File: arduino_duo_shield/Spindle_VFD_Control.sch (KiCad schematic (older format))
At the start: 25 parts, among them K2 JQC-3F, K3 JQC-3F, Q3 2N7000, Q4 BS250, Q5 2N7000, Q6 2N7000, U7 PC817, U8 PC817, U9 PC817

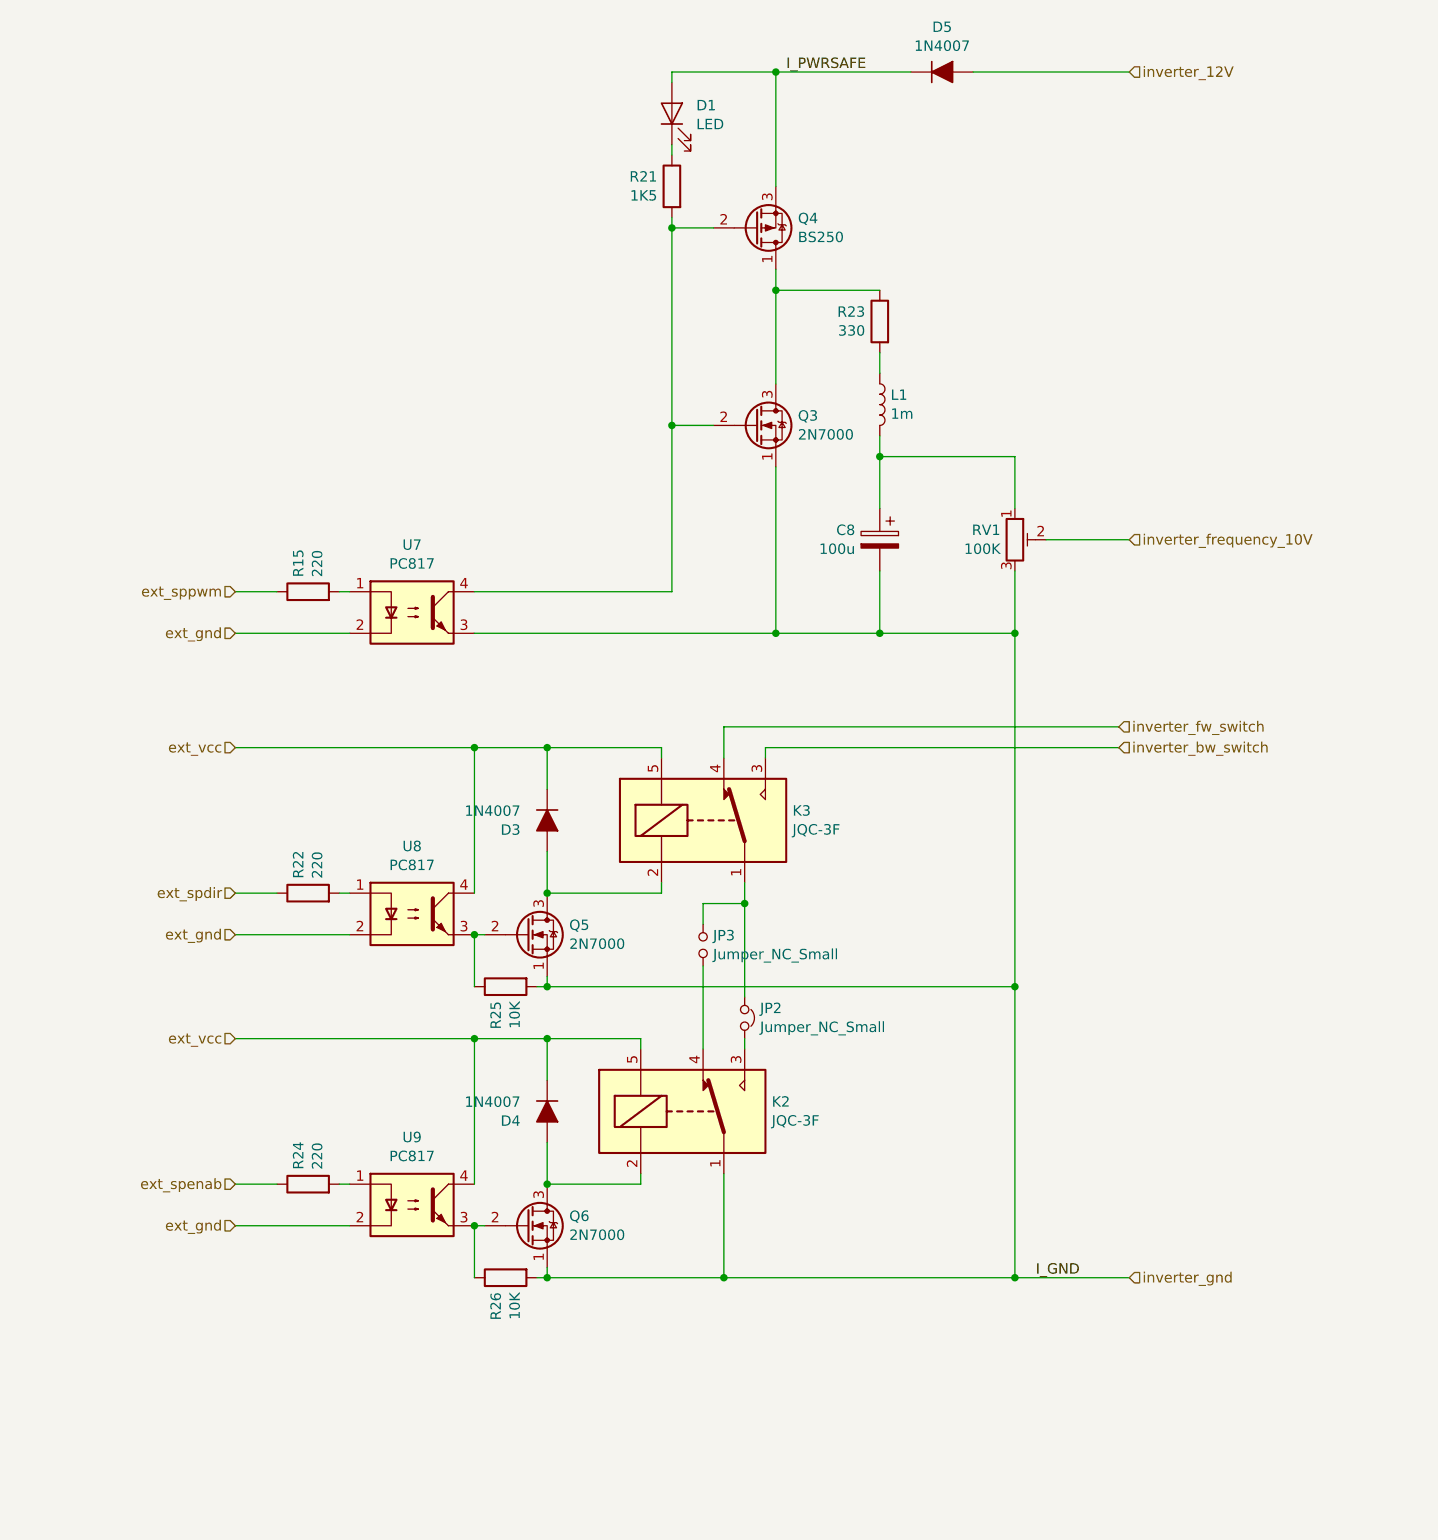
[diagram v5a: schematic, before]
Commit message: Add voltage follower as end stage of spindle control
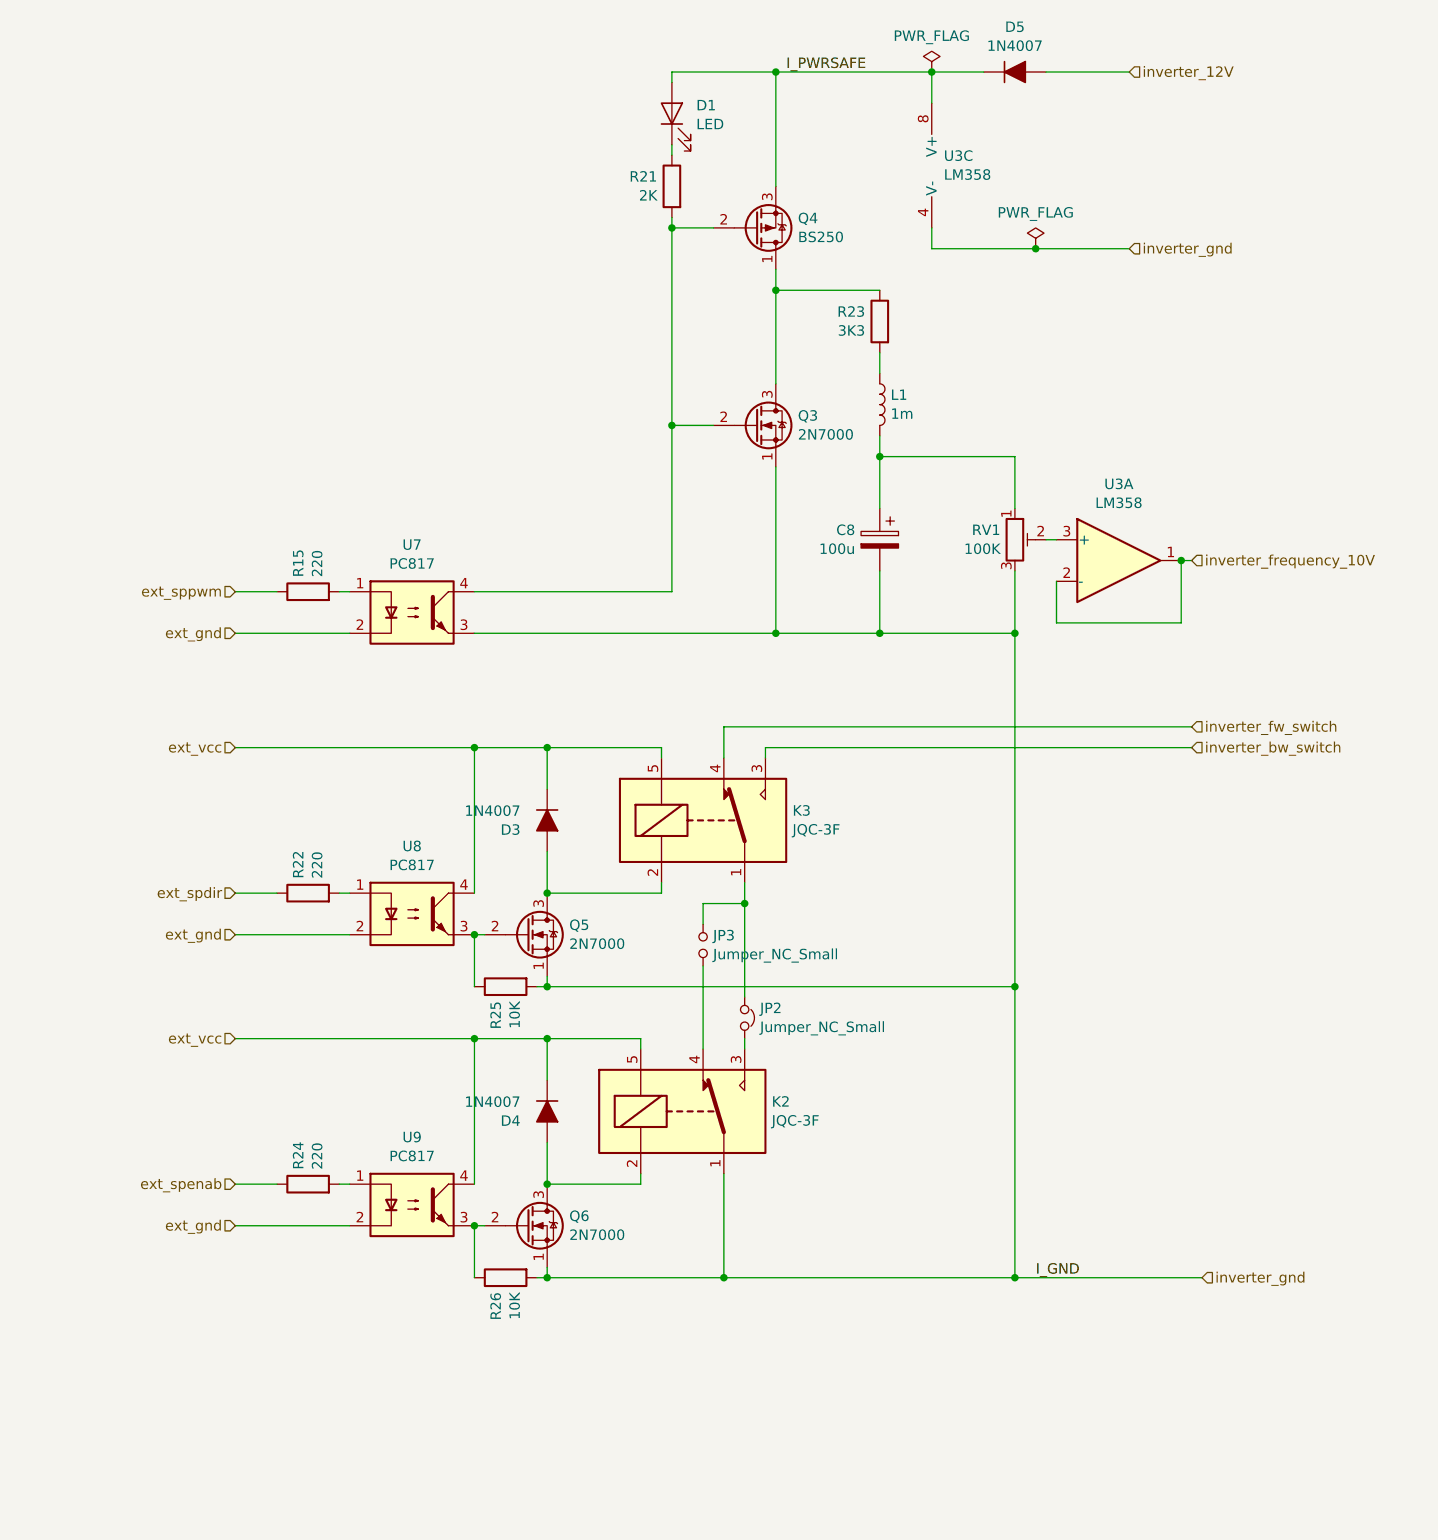
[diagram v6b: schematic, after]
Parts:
- added U3: LM358, Package_DIP:DIP-8_W7.62mm_Socket, symbol Amplifier_Operational:LM358
- R21: value 1K5 -> 2K
- R23: value 330 -> 3K3
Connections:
- net I_PWRSAFE: now also U3.8 (V+)
- net inverter_frequency_10V: now also U3.1, U3.2 (-); no longer RV1.2
- net inverter_gnd: now also U3.4 (V-)
- new net: RV1.2, U3.3 (+)
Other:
- moved on the sheet: D5
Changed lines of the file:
@@
 AR Path="/5DD17641/5DD6EE33" Ref="R23"  Part="1"
 F 0 "R23" H 5120 2046 50  0000 L CNN
-F 1 "330" H 5120 1955 50  0000 L CNN
+F 1 "3K3" H 5120 1955 50  0000 L CNN
 F 2 "Resistor_THT:R_Axial_DIN0309_L9.0mm_D3.2mm_P12.70mm_Horizontal" V 4980 2000 50  0001 C CNN
 F 3 "~" H 5050 2000 50  0001 C CNN
@@
 Wire Wire Line
 	2450 3300 2500 3300
-Text HLabel 6250 3050 2    50   Input ~ 0
+Text HLabel 6550 3150 2    50   Input ~ 0
 inverter_frequency_10V
 $Comp
@@
 AR Path="/5DD17641/5DD63534" Ref="R21"  Part="1"
 F 0 "R21" H 4120 1396 50  0000 L CNN
-F 1 "1K5" H 4120 1305 50  0000 L CNN
+F 1 "2K" H 4120 1305 50  0000 L CNN
 F 2 "Resistor_THT:R_Axial_DIN0207_L6.3mm_D2.5mm_P7.62mm_Horizontal" V 3980 1350 50  0001 C CNN
 F 3 "~" H 4050 1350 50  0001 C CNN
@@
 	4250 2500 4050 2500
 Wire Wire Line
-	6250 800  5500 800
-Wire Wire Line
 	4550 1350 4550 800
 Connection ~ 4550 800
@@
 	5050 3500 5700 3500
 Connection ~ 5050 3500
-Wire Wire Line
-	5850 3050 6250 3050
 $Comp
 L Device:R_POT_TRIM RV1
@@
 L Device:D_ALT D5
 U 1 1 5DE3902E
-P 5350 800
-F 0 "D5" H 5350 1016 50  0000 C CNN
-F 1 "1N4007" H 5350 925 50  0000 C CNN
-F 2 "Diode_THT:D_A-405_P7.62mm_Horizontal" H 5350 800 50  0001 C CNN
-F 3 "~" H 5350 800 50  0001 C CNN
-	1    5350 800
-	1    0    0    -1
-$EndComp
-Wire Wire Line
-	5200 800  4550 800
+P 5700 800
+F 0 "D5" H 5700 1016 50  0000 C CNN
+F 1 "1N4007" H 5700 925 50  0000 C CNN
+F 2 "Diode_THT:D_A-405_P7.62mm_Horizontal" H 5700 800 50  0001 C CNN
+F 3 "~" H 5700 800 50  0001 C CNN
+	1    5700 800
+	1    0    0    -1
+$EndComp
 $Comp
 L Relay:G5LE-1 K?
@@
 Wire Wire Line
 	3100 5450 3450 5450
-Text HLabel 6200 3950 2    50   Input ~ 0
+Text HLabel 6550 3950 2    50   Input ~ 0
 inverter_fw_switch
-Text HLabel 6200 4050 2    50   Input ~ 0
+Text HLabel 6550 4050 2    50   Input ~ 0
 inverter_bw_switch
-Text HLabel 6250 6600 2    50   Input ~ 0
+Text HLabel 6600 6600 2    50   Input ~ 0
 inverter_gnd
 Wire Wire Line
@@
 	1950 6350 2500 6350
 Wire Wire Line
-	6200 3950 4300 3950
+	6550 3950 4300 3950
 Wire Wire Line
 	4300 3950 4300 4100
 Wire Wire Line
-	6200 4050 4500 4050
+	6550 4050 4500 4050
 Wire Wire Line
 	4500 4050 4500 4100
@@
 Connection ~ 5700 6600
 Wire Wire Line
-	5700 6600 6250 6600
+	5700 6600 6600 6600
 Wire Wire Line
 	3450 5450 3450 5650
@@
 	0    -1   -1   0
 $EndComp
+$Comp
+L Amplifier_Operational:LM358 U3
+U 1 1 5E168C58
+P 6200 3150
+F 0 "U3" H 6200 3517 50  0000 C CNN
+F 1 "LM358" H 6200 3426 50  0000 C CNN
+F 2 "Package_DIP:DIP-8_W7.62mm_Socket" H 6200 3150 50  0001 C CNN
+F 3 "http://www.ti.com/lit/ds/symlink/lm2904-n.pdf" H 6200 3150 50  0001 C CNN
+	1    6200 3150
+	1    0    0    -1
+$EndComp
+Wire Wire Line
+	6500 3150 6550 3150
+Wire Wire Line
+	5850 3050 5900 3050
+Wire Wire Line
+	6500 3150 6500 3450
+Wire Wire Line
+	6500 3450 5900 3450
+Wire Wire Line
+	5900 3450 5900 3250
+Connection ~ 6500 3150
+Connection ~ 5300 800
+Wire Wire Line
+	5300 800  4550 800
+Text HLabel 6250 1650 2    50   Input ~ 0
+inverter_gnd
+Wire Wire Line
+	5550 800  5300 800
+Wire Wire Line
+	5850 800  6250 800
+Wire Wire Line
+	5300 800  5300 950
+Wire Wire Line
+	5300 1650 5800 1650
+Wire Wire Line
+	5300 1650 5300 1550
+$Comp
+L Amplifier_Operational:LM358 U3
+U 3 1 5E193DCF
+P 5400 1250
+F 0 "U3" H 5358 1296 50  0000 L CNN
+F 1 "LM358" H 5358 1205 50  0000 L CNN
+F 2 "Package_DIP:DIP-8_W7.62mm_Socket" H 5400 1250 50  0001 C CNN
+F 3 "http://www.ti.com/lit/ds/symlink/lm2904-n.pdf" H 5400 1250 50  0001 C CNN
+	3    5400 1250
+	1    0    0    -1
+$EndComp
+$Comp
+L power:PWR_FLAG #FLG0101
+U 1 1 5E16F505
+P 5300 800
+F 0 "#FLG0101" H 5300 875 50  0001 C CNN
+F 1 "PWR_FLAG" H 5300 973 50  0000 C CNN
+F 2 "" H 5300 800 50  0001 C CNN
+F 3 "~" H 5300 800 50  0001 C CNN
+	1    5300 800
+	1    0    0    -1
+$EndComp
+$Comp
+L power:PWR_FLAG #FLG0102
+U 1 1 5E170449
+P 5800 1650
+F 0 "#FLG0102" H 5800 1725 50  0001 C CNN
+F 1 "PWR_FLAG" H 5800 1823 50  0000 C CNN
+F 2 "" H 5800 1650 50  0001 C CNN
+F 3 "~" H 5800 1650 50  0001 C CNN
+	1    5800 1650
+	1    0    0    -1
+$EndComp
+Connection ~ 5800 1650
+Wire Wire Line
+	5800 1650 6250 1650
 $EndSCHEMATC

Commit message: Expose raw analog frequency control
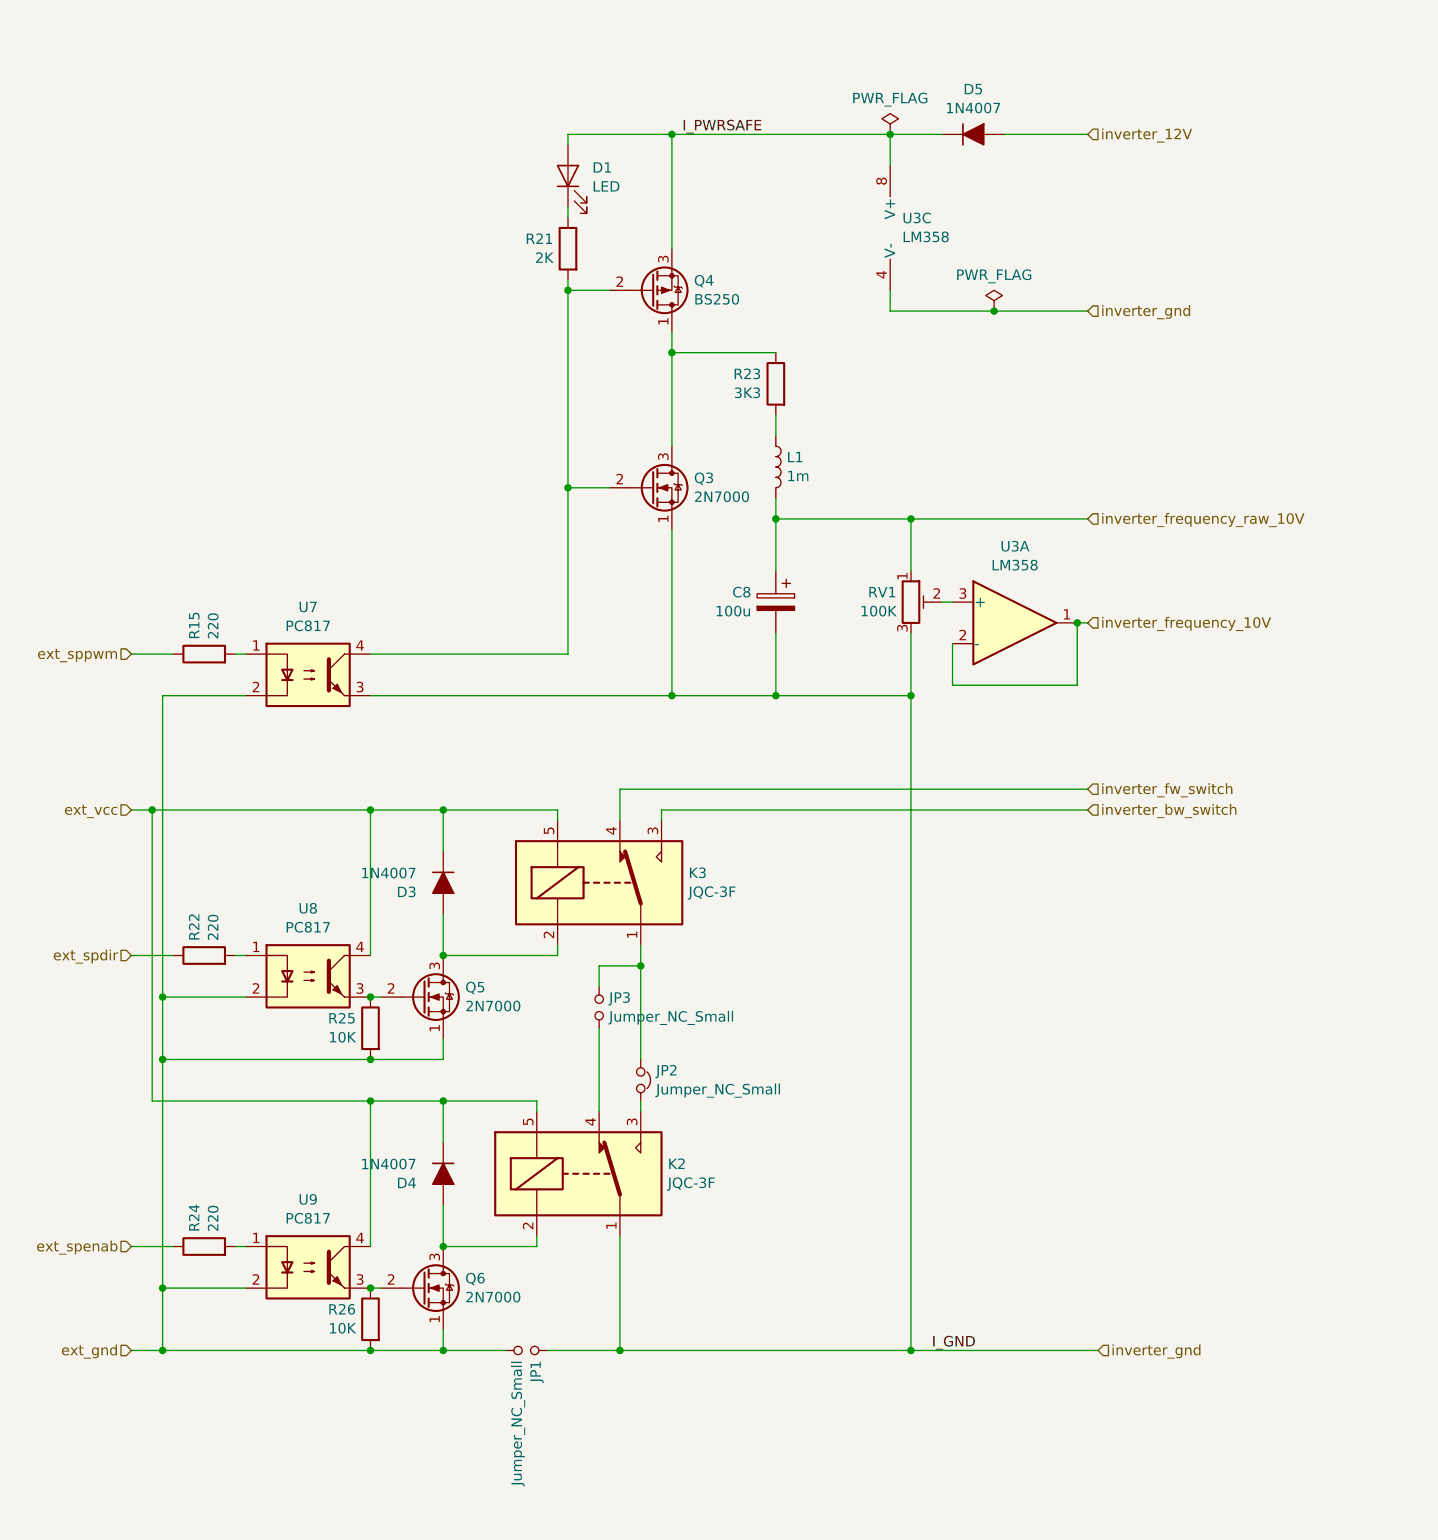
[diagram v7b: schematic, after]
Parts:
- added JP1: Jumper_NC_Small, Connector_PinHeader_2.54mm:PinHeader_1x02_P2.54mm_Vertical, symbol Device:Jumper_NO_Small
- Q3, Q4, Q5, Q6: footprint Package_TO_SOT_THT:TO-92_Inline -> Package_TO_SOT_THT:TO-92_Wide
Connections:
- net ext_gnd: now also Q5.1 (S), Q6.1 (S), R25.2, R26.2, JP1.2
- net inverter_gnd: now also JP1.1; no longer Q5.1 (S), Q6.1 (S), R25.2, R26.2
- net inverter_frequency_raw_10V: now reaches C8.1, L1.2, RV1.1
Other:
- moved on the sheet: C8, D1, D3, D4, D5, JP2, JP3, K2, K3, L1, Q3, Q4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
